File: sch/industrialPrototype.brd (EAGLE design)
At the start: 160 x 100 mm, 11 parts, among them IC1 LD1117V33C, U1 PIC16F1825-I/SL

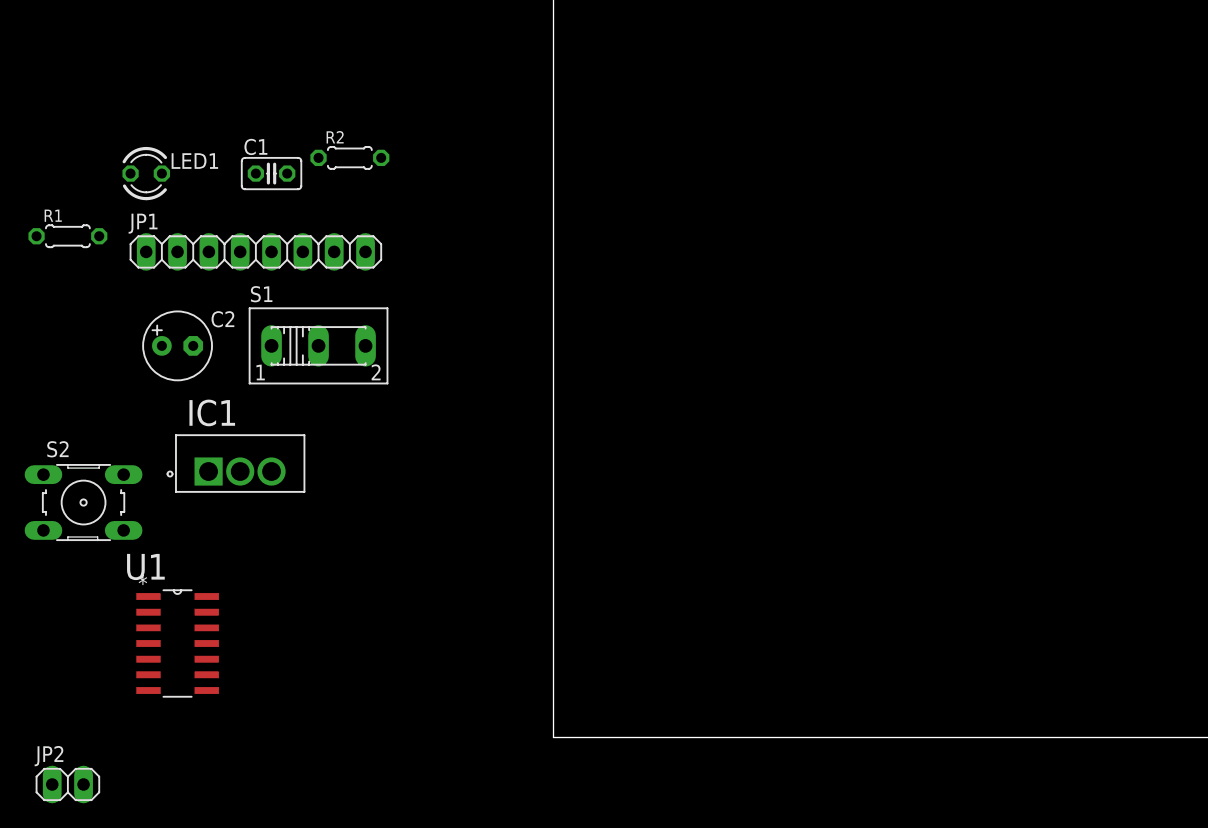
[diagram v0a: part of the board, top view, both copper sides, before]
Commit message: Added Programming Header. Placed components on PCB. Routing still has to be done
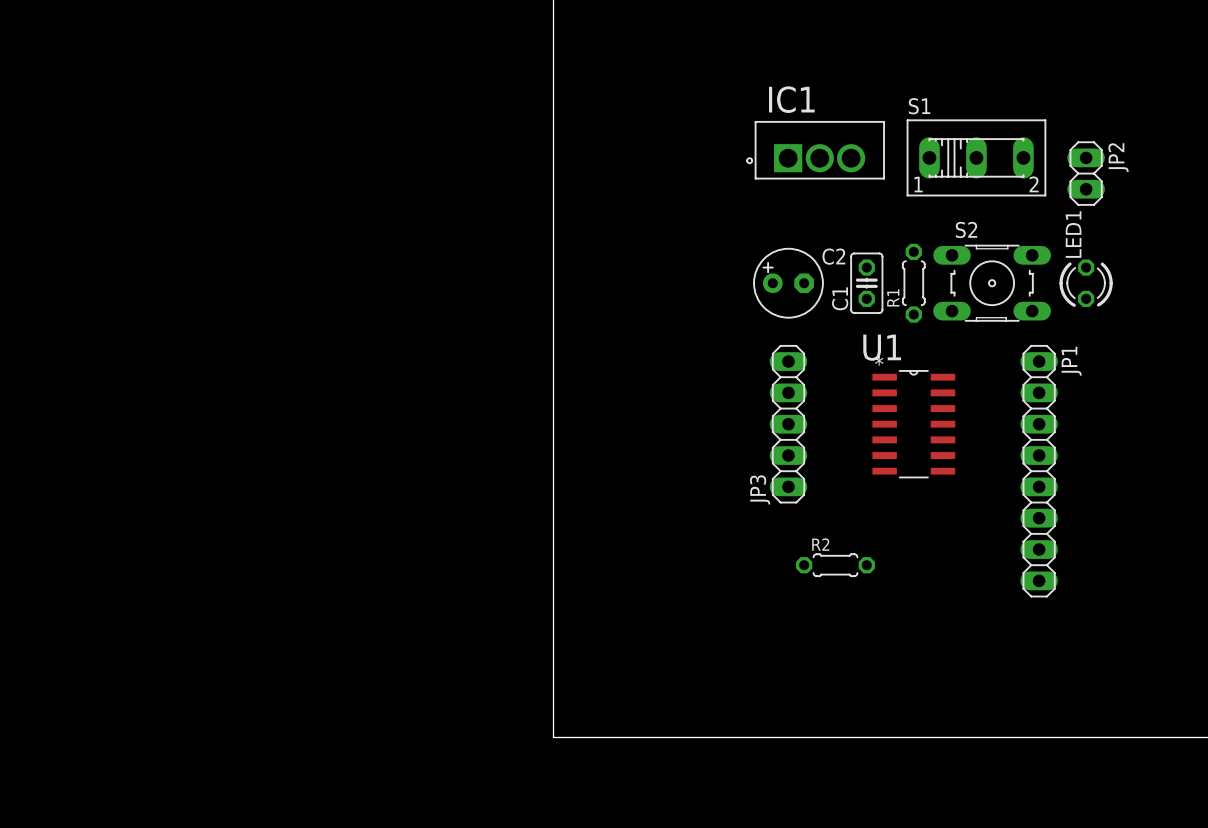
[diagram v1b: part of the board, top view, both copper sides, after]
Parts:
- added JP3: (no value), pinhead:1X05
- C1: value (none) -> 47n
- C2: value (none) -> 47u
- moved JP2 96.3 mm to (43.2, 45.7), turned to 270 degrees
- moved LED1 76.7 mm to (43.2, 36.8), turned to 90 degrees
- moved S2 75.8 mm to (35.6, 36.8)
- moved R1 68.7 mm to (29.2, 36.8), turned to 90 degrees
- moved JP1 65.9 mm to (39.4, 21.6), turned to 270 degrees
- moved U1 62.3 mm to (29.2, 25.4)
- moved S1 55.5 mm to (34.3, 47.0)
- moved IC1 53.4 mm to (24.1, 48.3)
- moved R2 51.4 mm to (22.9, 14.0)
- moved C2 49.8 mm to (19.1, 36.8)
- moved C1 49.1 mm to (25.4, 36.8), turned to 90 degrees
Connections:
- net !MCLR!: now also JP3.1
- net 3V3: now also JP3.2
- net GND: now also JP3.3
- net ICSPCLK: now also JP3.5
- net ICSPDAT: now also JP3.4
